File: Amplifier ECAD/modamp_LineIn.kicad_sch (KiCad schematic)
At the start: 7 parts, among them U2 MCP6004

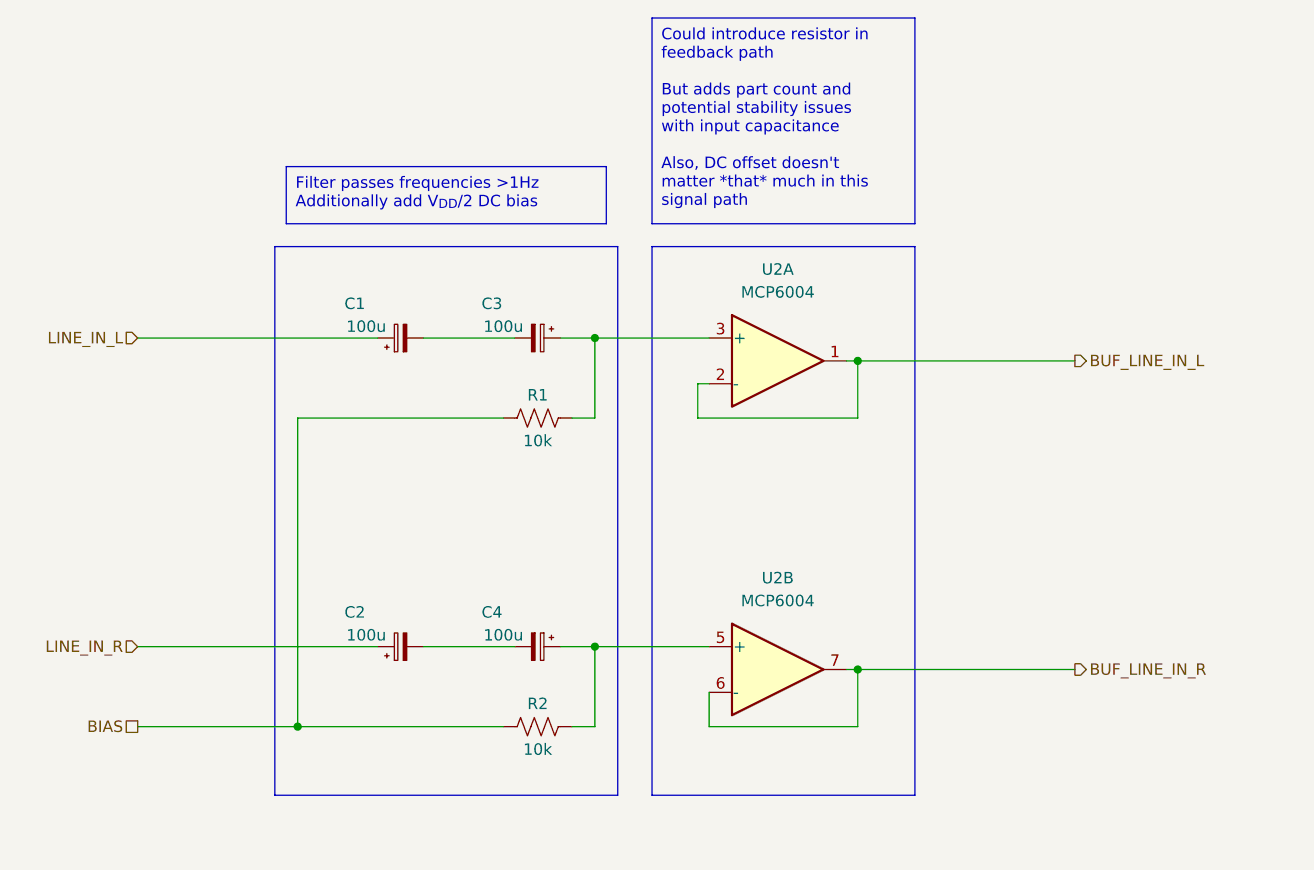
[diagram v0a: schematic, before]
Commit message: File renaming; updating supplier references
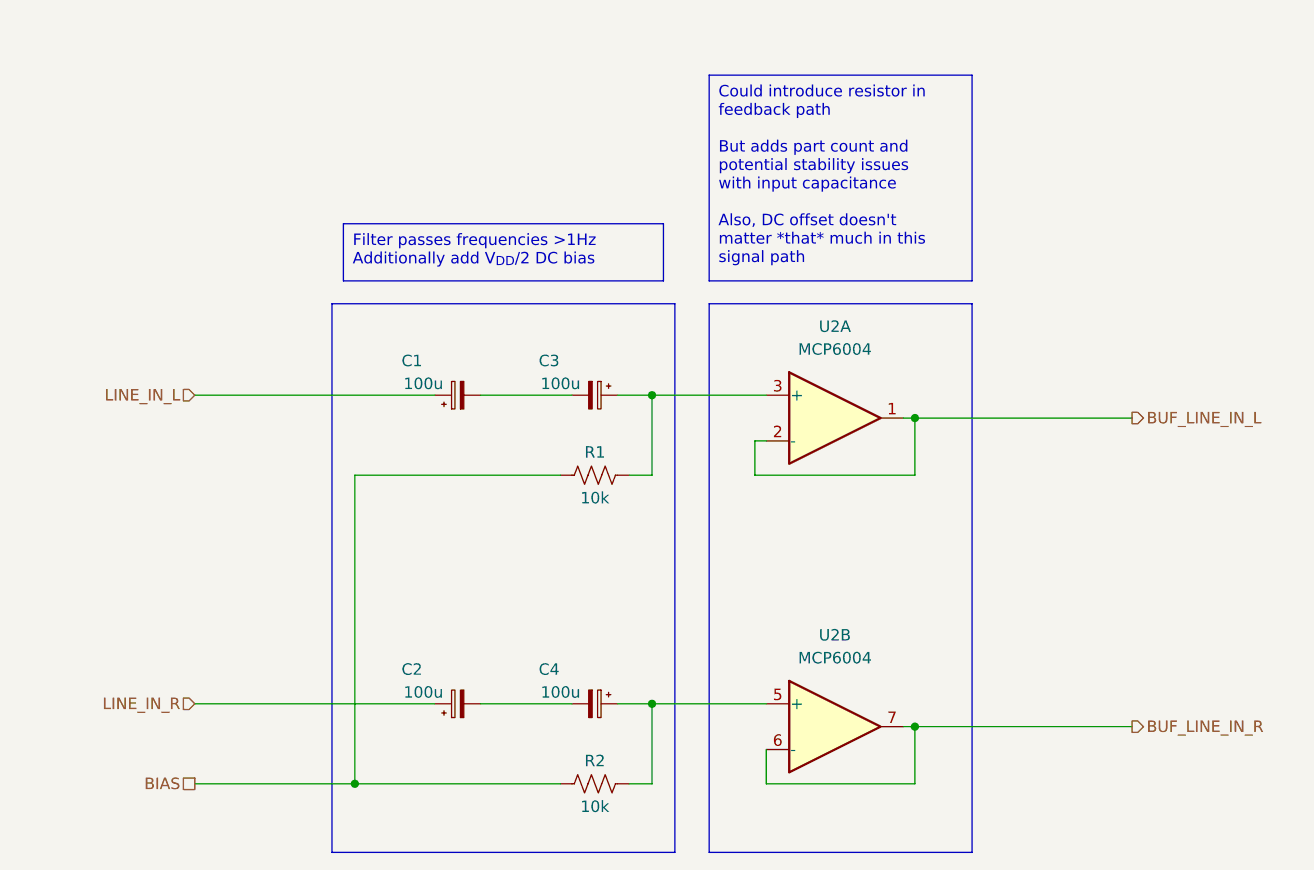
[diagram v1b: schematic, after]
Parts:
- C1, C2, C3, C4: footprint Custom-RLC:CP_Radial_D6.3mm_H12.5_P2.50mm -> Custom-RLC:CP_KEMET_ESY; symbol Custom-CapacitorTHT:860020473008 -> Custom-CapacitorTHT:ESY107M025AE3AA; Manufacturer Würth Elektronik -> KEMET; Part Number 860020473008 -> ESY107M025AE3AA
- R1, R2: symbol Custom-ResistorTHT:MFR-25FRF52-10K -> Custom-ResistorTHT:CF14JT10K0; Manufacturer YAGEO -> Stackpole Electronics Inc; Part Number MFR-25FRF52-10K -> CF14JT10K0
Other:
- moved on the sheet: C1, C2, C3, C4, R1, R2, U2A, U2B
